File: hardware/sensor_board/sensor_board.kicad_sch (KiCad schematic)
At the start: 8 parts

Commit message: all bricked...
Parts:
- removed C? (x3): C, symbol Device:C
- removed R?: R, symbol Device:R
- removed U?: PESD2CAN, symbol ownLib:PESD2CAN
- added C1, C8: 10u / 10V, symbol Device:C
- added C2, C3, C7: 100n / 10V, symbol Device:C
- added C4, C5: 18p, symbol Device:C
- added C6: 1u / 10V, symbol Device:C
- added D1: RCLAMP0502BA, Package_TO_SOT_SMD:SOT-416, symbol Power_Protection:RCLAMP0502BA
- added J1: CORTEX-SWD-6, footprints:TC2030-IDC-NL, symbol ownLib:CORTEX-SWD-6
- added Q1, Q2: Q_NMOS_DGS, symbol Device:Q_PMOS_GSD
- added R1: 2k2, symbol Device:R
- added R2, R3, R4, R5: R, symbol Device:R
- added U1: ATSAMC21E17A, Package_DFN_QFN:QFN-32-1EP_5x5mm_P0.5mm_EP3.6x3.6mm, symbol ownLib:ATSAMC21E17A
- added Y1: Crystal, symbol Device:Crystal
- R6: renamed from R?; value R -> 120R
- gave numbers to parts that had none: 2
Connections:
- net CAN+: now also R6.2, U2.7 (CANH), D1.1 (K1)
- net CAN-: now also D1.2 (K2)
- net CAN_{RX}: now also U1.23 (PA24)
- net CAN_{TX}: now also U1.22 (PA23)
- net GND: now also C1.2, C2.2, C3.2, C4.1, C5.1, C6.2, C7.2, C8.2, D1.3 (A), J1.5 (GND), U1.10 (GND), U1.28 (GND)
- net VDD: now also C1.1, C2.1, C3.1, C8.1, J1.1 (VCC), Q2.2 (S), R1.1, R5.2, U1.30 (VDDIN), U1.9 (VDDANA)
- new net: Q2.1 (G), R3.2, R5.1
- new net: Q1.1 (G), R2.2, R4.1
- new net: C6.1, C7.1, U1.29 (VDDCORE)
- new net +5V: Q1.2 (S), R4.2
- new net 5VSW: Q1.3 (D)
- new net 5VSW_SIG: R2.1, U1.4 (PA03)
- new net CO2CAL: U1.6 (PA05)
- new net I2C.SCL: U1.12 (PA09)
- new net I2C.SDA: U1.11 (PA08)
- new net SWCLK: J1.4 (SWCLK), U1.31 (PA30)
- new net SWDIO: J1.2 (SWDIO), U1.32 (PA31)
- new net UART.RX: U1.2 (PA01)
- new net UART.TX: U1.1 (PA00)
- new net VDDSW: Q2.3 (D)
- new net VDDSW_SIG: R3.1, U1.5 (PA04)
- new net X_{IN}: C4.2, U1.15 (PA14), Y1.2
- new net X_{OUT}: C5.2, U1.16 (PA15), Y1.1
- new net ~{RESET}: J1.3 (nRESET), R1.2, U1.26 (~{RESET})
- no-connect marks 0 -> 14
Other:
- sheet Power ports: added none; removed SWD{SWO SWCLK SWDIO}
- moved on the sheet: J2, R6, U2

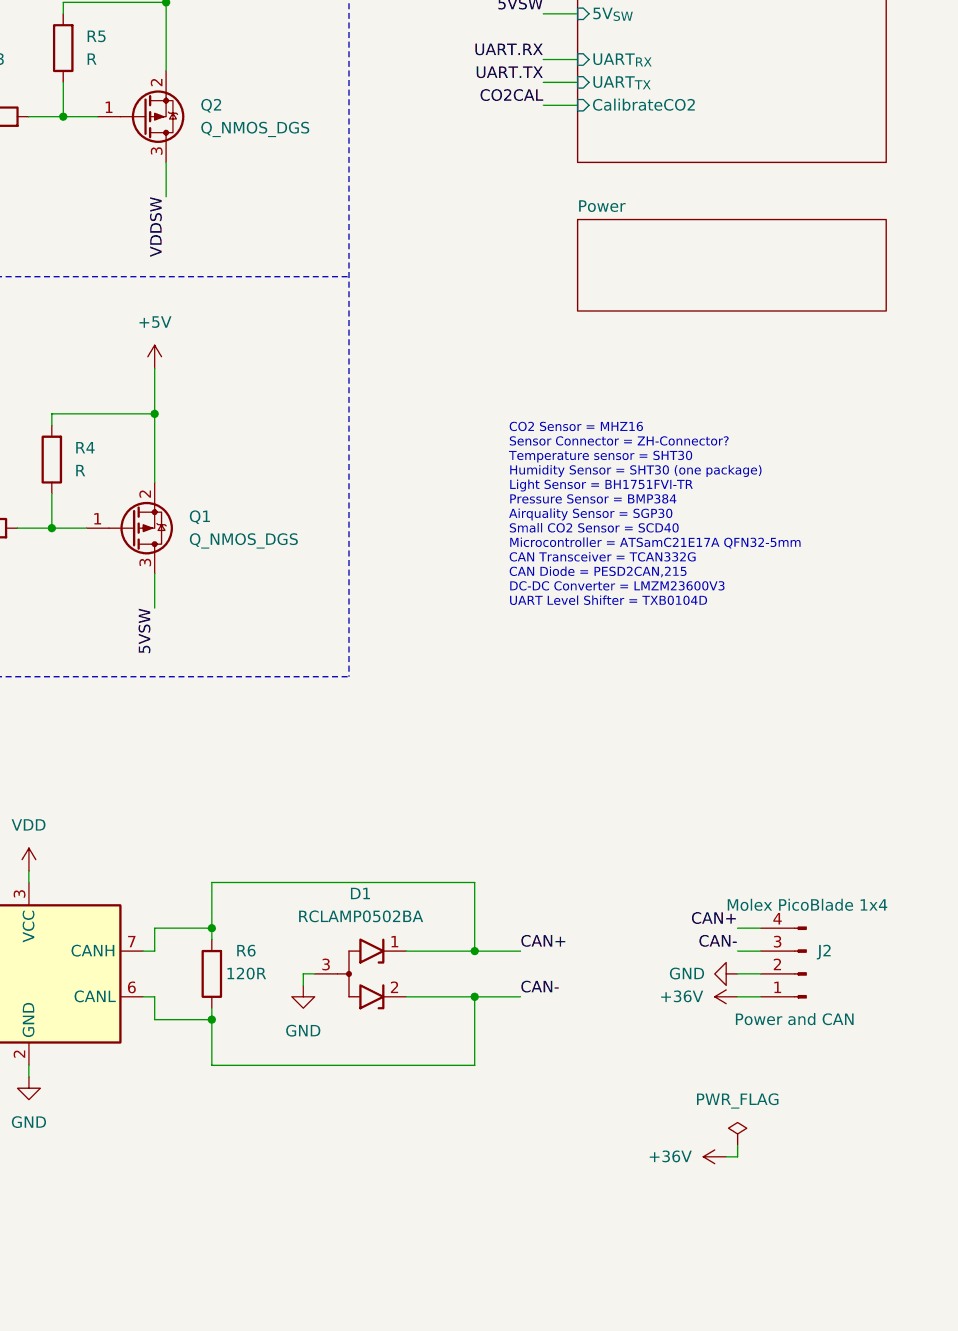
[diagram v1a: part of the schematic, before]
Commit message: solved issues with ERC
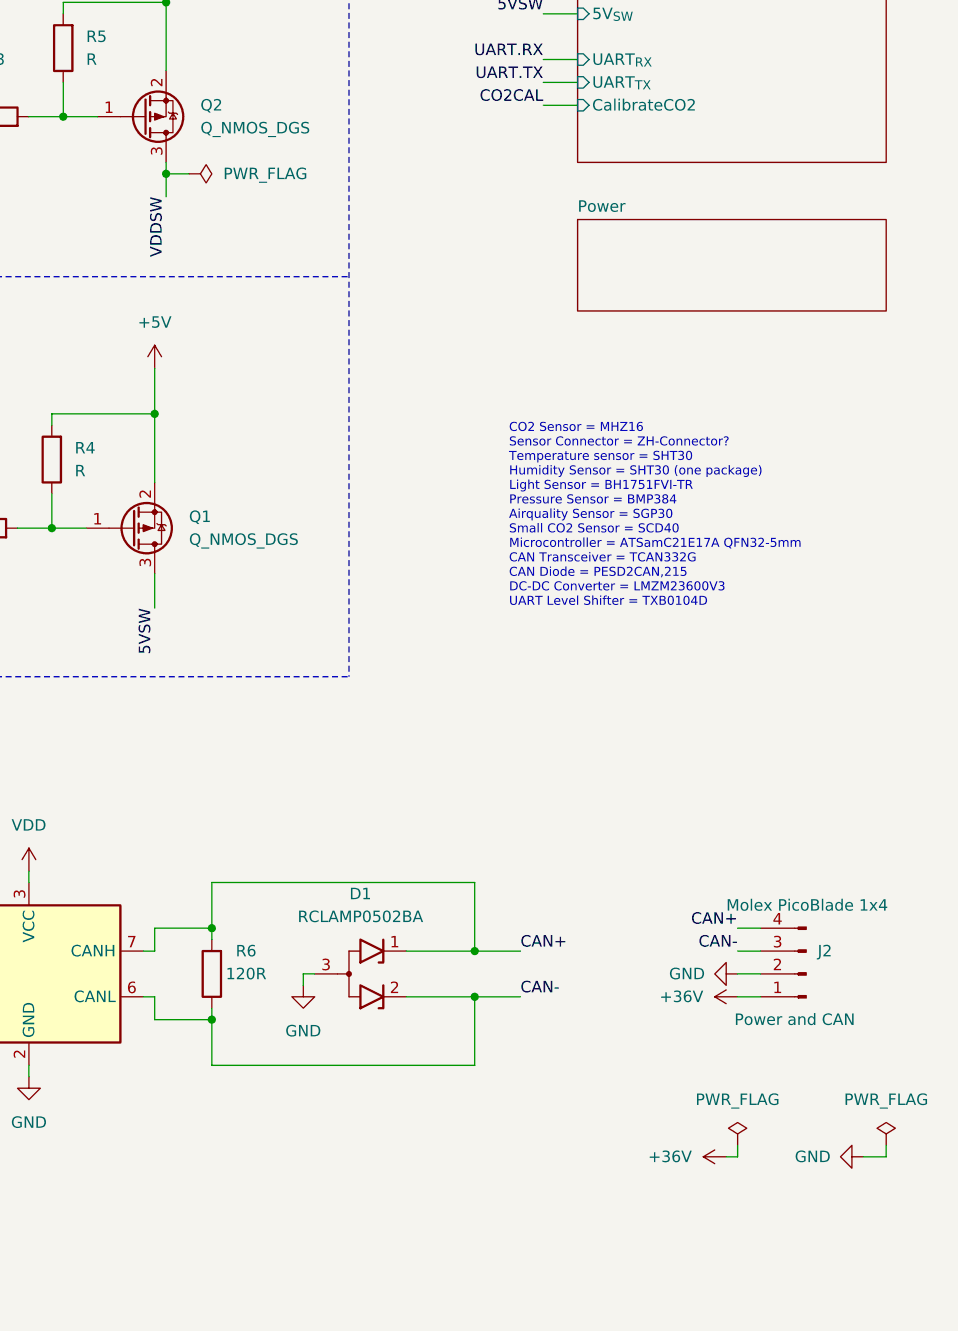
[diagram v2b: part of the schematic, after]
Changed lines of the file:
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@@
   (junction (at 193.04 80.01) (diameter 0) (color 0 0 0 0))
   (junction (at 194.31 34.29) (diameter 0) (color 0 0 0 0))
+  (junction (at 194.31 53.34) (diameter 0) (color 0 0 0 0))
   (junction (at 199.39 137.16) (diameter 0) (color 0 0 0 0))
   (junction (at 199.39 147.32) (diameter 0) (color 0 0 0 0))
@@
     (stroke (width 0) (type solid) (color 0 0 0 0))
   )
-  (wire (pts (xy 194.31 52.07) (xy 194.31 55.88))
+  (wire (pts (xy 194.31 52.07) (xy 194.31 53.34))
+    (stroke (width 0) (type solid) (color 0 0 0 0))
+  )
+  (wire (pts (xy 194.31 53.34) (xy 194.31 55.88))
+    (stroke (width 0) (type solid) (color 0 0 0 0))
+  )
+  (wire (pts (xy 194.31 53.34) (xy 196.85 53.34))
     (stroke (width 0) (type solid) (color 0 0 0 0))
   )
@@
   )
   (wire (pts (xy 257.81 162.56) (xy 257.81 161.29))
+    (stroke (width 0) (type solid) (color 0 0 0 0))
+  )
+  (wire (pts (xy 271.78 162.56) (xy 274.32 162.56))
+    (stroke (width 0) (type solid) (color 0 0 0 0))
+  )
+  (wire (pts (xy 274.32 162.56) (xy 274.32 161.29))
     (stroke (width 0) (type solid) (color 0 0 0 0))
   )
@@
     (pin "1")
   )
+  (symbol (lib_id "power:PWR_FLAG") (at 196.85 53.34 270) (unit 1)
+    (in_bom yes) (on_board yes) (fields_autoplaced)
+    (property "Reference" "#FLG01" (id 0) (at 198.755 53.34 0)
+      (effects (font (size 1.27 1.27)) hide)
+    )
+    (property "Value" "PWR_FLAG" (id 1) (at 200.66 53.3399 90)
+      (effects (font (size 1.27 1.27)) (justify left))
+    )
+    (property "Footprint" "" (id 2) (at 196.85 53.34 0)
+      (effects (font (size 1.27 1.27)) hide)
+    )
+    (property "Datasheet" "~" (id 3) (at 196.85 53.34 0)
+      (effects (font (size 1.27 1.27)) hide)
+    )
+    (pin "1")
+  )
   (symbol (lib_id "power:PWR_FLAG") (at 257.81 161.29 0) (unit 1)
     (in_bom yes) (on_board yes) (fields_autoplaced)
@@
     )
     (property "Datasheet" "~" (id 3) (at 257.81 161.29 0)
+      (effects (font (size 1.27 1.27)) hide)
+    )
+    (pin "1")
+  )
+  (symbol (lib_id "power:PWR_FLAG") (at 274.32 161.29 0) (unit 1)
+    (in_bom yes) (on_board yes) (fields_autoplaced)
+    (property "Reference" "#FLG0102" (id 0) (at 274.32 159.385 0)
+      (effects (font (size 1.27 1.27)) hide)
+    )
+    (property "Value" "PWR_FLAG" (id 1) (at 274.32 156.21 0))
+    (property "Footprint" "" (id 2) (at 274.32 161.29 0)
+      (effects (font (size 1.27 1.27)) hide)
+    )
+    (property "Datasheet" "~" (id 3) (at 274.32 161.29 0)
       (effects (font (size 1.27 1.27)) hide)
     )
@@
     )
     (property "Datasheet" "" (id 3) (at 257.81 142.24 0)
+      (effects (font (size 1.27 1.27)) hide)
+    )
+    (pin "1")
+  )
+  (symbol (lib_id "power:GND") (at 271.78 162.56 270) (unit 1)
+    (in_bom yes) (on_board yes)
+    (property "Reference" "#PWR0102" (id 0) (at 265.43 162.56 0)
+      (effects (font (size 1.27 1.27)) hide)
+    )
+    (property "Value" "GND" (id 1) (at 264.16 162.5599 90)
+      (effects (font (size 1.27 1.27)) (justify left))
+    )
+    (property "Footprint" "" (id 2) (at 271.78 162.56 0)
+      (effects (font (size 1.27 1.27)) hide)
+    )
+    (property "Datasheet" "" (id 3) (at 271.78 162.56 0)
       (effects (font (size 1.27 1.27)) hide)
     )
@@
   )
   (symbol_instances
+    (path "/3e86196d-7be5-4f72-a075-4619159f1c7f"
+      (reference "#FLG01") (unit 1) (value "PWR_FLAG") (footprint "")
+    )
     (path "/1d3ecf29-19a5-423b-9e86-10e11573b1b7"
       (reference "#FLG0101") (unit 1) (value "PWR_FLAG") (footprint "")
     )
+    (path "/74761b04-2e0e-48bc-8cd2-df69861a8420"
+      (reference "#FLG0102") (unit 1) (value "PWR_FLAG") (footprint "")
+    )
     (path "/8306a43a-0f6c-479d-b1d9-b6e95367aa2c"
       (reference "#PWR01") (unit 1) (value "VDD") (footprint "")
@@
       (reference "#PWR024") (unit 1) (value "GND") (footprint "")
     )
-    (path "/c4dbf479-cf2f-484d-ade6-def83986d8b6/b34e0c88-73d0-4fb3-a9d7-701d175303e9"
-      (reference "#PWR025") (unit 1) (value "VDD") (footprint "")
-    )
     (path "/c4dbf479-cf2f-484d-ade6-def83986d8b6/e44e48f3-3b0a-4d06-ba81-f082667f0867"
       (reference "#PWR026") (unit 1) (value "GND") (footprint "")
@@
       (reference "#PWR027") (unit 1) (value "GND") (footprint "")
     )
-    (path "/c4dbf479-cf2f-484d-ade6-def83986d8b6/c01d8e07-19b0-49c3-91c0-1c6475a0896f"
-      (reference "#PWR028") (unit 1) (value "VDD") (footprint "")
-    )
-    (path "/c4dbf479-cf2f-484d-ade6-def83986d8b6/fb54e666-356e-4647-8a05-d0c8bf4234d4"
-      (reference "#PWR029") (unit 1) (value "VDD") (footprint "")
-    )
     (path "/c4dbf479-cf2f-484d-ade6-def83986d8b6/811bdb1d-8b3c-44ab-924c-e552095907d7"
       (reference "#PWR030") (unit 1) (value "GND") (footprint "")
@@
       (reference "#PWR038") (unit 1) (value "GND") (footprint "")
     )
-    (path "/5266303c-cc26-4361-a3c7-41c3c779268d/5ea51cc6-628a-4b08-881b-78cf8dbcec67"
-      (reference "#PWR039") (unit 1) (value "VDD") (footprint "")
-    )
     (path "/adfd184c-f938-41aa-8cc3-19d2e60b847d"
       (reference "#PWR0101") (unit 1) (value "+36V") (footprint "")
     )
+    (path "/111fc8cc-7747-4f2e-9fcd-4c063190a483"
+      (reference "#PWR0102") (unit 1) (value "GND") (footprint "")
+    )
+    (path "/5266303c-cc26-4361-a3c7-41c3c779268d/4c9a339a-72e6-4346-b113-de4a084399ac"
+      (reference "#PWR0103") (unit 1) (value "+5V") (footprint "")
+    )
     (path "/cea51140-d1a5-4498-ac28-6d3c6af90a7f"
       (reference "C1") (unit 1) (value "10u / 10V") (footprint "")
@@
       (reference "U4") (unit 1) (value "SHT30-DIS") (footprint "Sensor_Humidity:Sensirion_DFN-8-1EP_2.5x2.5mm_P0.5mm_EP1.1x1.7mm")
     )
-    (path "/c4dbf479-cf2f-484d-ade6-def83986d8b6/2713ac11-4919-4bfe-87f5-9e015b3083d0"
-      (reference "U5") (unit 1) (value "BMP384") (footprint "")
-    )
-    (path "/c4dbf479-cf2f-484d-ade6-def83986d8b6/72869bcb-c605-4b0f-9b78-a3c7d0346b20"
-      (reference "U6") (unit 1) (value "SCD40") (footprint "")
-    )
-    (path "/c4dbf479-cf2f-484d-ade6-def83986d8b6/bcd0e211-90eb-41d5-bf7f-31ace572862e"
+    (path "/c4dbf479-cf2f-484d-ade6-def83986d8b6/f453ff1f-a773-45fc-ae5c-94711b2be9d1"
+      (reference "U5") (unit 1) (value "BMP384") (footprint "dp:BMP384")
+    )
+    (path "/c4dbf479-cf2f-484d-ade6-def83986d8b6/0afe84fd-9a71-4e85-ba4a-ded33ce31373"
+      (reference "U6") (unit 1) (value "SCD4x") (footprint "dp:SCD4x")
+    )
+    (path "/c4dbf479-cf2f-484d-ade6-def83986d8b6/0544bcc2-7380-4571-bf84-ab641f79cefc"
       (reference "U7") (unit 1) (value "SGP30") (footprint "")
     )

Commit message: did some stuff
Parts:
- C1, C2, C3, C4, C5, C6, C7, C8: footprint (none) -> Capacitor_SMD:C_0603_1608Metric
- J2: footprint (none) -> Connector_Molex:Molex_PicoBlade_53261-0471_1x04-1MP_P1.25mm_Horizontal
- Q1, Q2: value Q_NMOS_DGS -> SI2337DS-T1-BE3; footprint (none) -> Package_TO_SOT_SMD:SOT-23
- R1: footprint (none) -> Resistor_SMD:R_0603_1608Metric
- R2, R3: value R -> 100R; footprint (none) -> Resistor_SMD:R_0603_1608Metric
- R4, R5: value R -> 10k; footprint (none) -> Resistor_SMD:R_0603_1608Metric
- R6: footprint (none) -> Resistor_SMD:R_1206_3216Metric
- U2: footprint (none) -> Package_SO:SOIC-8_3.9x4.9mm_P1.27mm
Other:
- moved on the sheet: Q1, Q2, R2, R3, R4, R5

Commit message: finished schematic and added board
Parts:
- added H1, H2, H3, H4: MountingHole, MountingHole:MountingHole_3.2mm_M3, symbol Mechanical:MountingHole
- J1: footprint footprints:TC2030-IDC-NL -> Connector_Hirose:Hirose_DF11-6DP-2DSA_2x03_P2.00mm_Vertical
- Y1: footprint (none) -> ownLib:Abracon_ABC2
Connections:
- net CAN+: now also J2.3 (Pin_3); no longer J2.4 (Pin_4)
- net CAN-: now also J2.4 (Pin_4); no longer J2.3 (Pin_3)
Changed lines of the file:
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@@
     (effects (font (size 1.27 1.27)) (justify right bottom))
   )
-  (label "CAN+" (at 257.81 137.16 180)
+  (label "CAN-" (at 257.81 137.16 180)
     (effects (font (size 1.27 1.27)) (justify right bottom))
   )
-  (label "CAN-" (at 257.81 139.7 180)
+  (label "CAN+" (at 257.81 139.7 180)
     (effects (font (size 1.27 1.27)) (justify right bottom))
   )
@@
     (pin "1")
   )
+  (symbol (lib_id "Mechanical:MountingHole") (at 158.75 177.8 0) (unit 1)
+    (in_bom yes) (on_board yes) (fields_autoplaced)
+    (property "Reference" "H1" (id 0) (at 161.29 176.5299 0)
+      (effects (font (size 1.27 1.27)) (justify left))
+    )
+    (property "Value" "MountingHole" (id 1) (at 161.29 179.0699 0)
+      (effects (font (size 1.27 1.27)) (justify left))
+    )
+    (property "Footprint" "MountingHole:MountingHole_3.2mm_M3" (id 2) (at 158.75 177.8 0)
+      (effects (font (size 1.27 1.27)) hide)
+    )
+    (property "Datasheet" "~" (id 3) (at 158.75 177.8 0)
+      (effects (font (size 1.27 1.27)) hide)
+    )
+  )
+  (symbol (lib_id "Mechanical:MountingHole") (at 158.75 182.88 0) (unit 1)
+    (in_bom yes) (on_board yes) (fields_autoplaced)
+    (property "Reference" "H2" (id 0) (at 161.29 181.6099 0)
+      (effects (font (size 1.27 1.27)) (justify left))
+    )
+    (property "Value" "MountingHole" (id 1) (at 161.29 184.1499 0)
+      (effects (font (size 1.27 1.27)) (justify left))
+    )
+    (property "Footprint" "MountingHole:MountingHole_3.2mm_M3" (id 2) (at 158.75 182.88 0)
+      (effects (font (size 1.27 1.27)) hide)
+    )
+    (property "Datasheet" "~" (id 3) (at 158.75 182.88 0)
+      (effects (font (size 1.27 1.27)) hide)
+    )
+  )
+  (symbol (lib_id "Mechanical:MountingHole") (at 158.75 187.96 0) (unit 1)
+    (in_bom yes) (on_board yes) (fields_autoplaced)
+    (property "Reference" "H3" (id 0) (at 161.29 186.6899 0)
+      (effects (font (size 1.27 1.27)) (justify left))
+    )
+    (property "Value" "MountingHole" (id 1) (at 161.29 189.2299 0)
+      (effects (font (size 1.27 1.27)) (justify left))
+    )
+    (property "Footprint" "MountingHole:MountingHole_3.2mm_M3" (id 2) (at 158.75 187.96 0)
+      (effects (font (size 1.27 1.27)) hide)
+    )
+    (property "Datasheet" "~" (id 3) (at 158.75 187.96 0)
+      (effects (font (size 1.27 1.27)) hide)
+    )
+  )
+  (symbol (lib_id "Mechanical:MountingHole") (at 158.75 193.04 0) (unit 1)
+    (in_bom yes) (on_board yes) (fields_autoplaced)
+    (property "Reference" "H4" (id 0) (at 161.29 191.7699 0)
+      (effects (font (size 1.27 1.27)) (justify left))
+    )
+    (property "Value" "MountingHole" (id 1) (at 161.29 194.3099 0)
+      (effects (font (size 1.27 1.27)) (justify left))
+    )
+    (property "Footprint" "MountingHole:MountingHole_3.2mm_M3" (id 2) (at 158.75 193.04 0)
+      (effects (font (size 1.27 1.27)) hide)
+    )
+    (property "Datasheet" "~" (id 3) (at 158.75 193.04 0)
+      (effects (font (size 1.27 1.27)) hide)
+    )
+  )
   (symbol (lib_id "Device:R") (at 40.64 160.02 0) (unit 1)
     (in_bom yes) (on_board yes) (fields_autoplaced)
@@
       (effects (font (size 1.27 1.27)) (justify right))
     )
-    (property "Footprint" "" (id 2) (at 109.22 166.37 0)
+    (property "Footprint" "ownLib:Abracon_ABC2" (id 2) (at 109.22 166.37 0)
       (effects (font (size 1.27 1.27)) hide)
     )
@@
     (property "Reference" "J1" (id 0) (at 57.15 181.61 0))
     (property "Value" "CORTEX-SWD-6" (id 1) (at 57.15 179.07 0))
-    (property "Footprint" "footprints:TC2030-IDC-NL" (id 2) (at 53.34 168.91 0)
+    (property "Footprint" "Connector_Hirose:Hirose_DF11-6DP-2DSA_2x03_P2.00mm_Vertical" (id 2) (at 53.34 168.91 0)
       (effects (font (size 1.27 1.27)) hide)
     )
@@
       (reference "#PWR021") (unit 1) (value "GND") (footprint "")
     )
-    (path "/c4dbf479-cf2f-484d-ade6-def83986d8b6/f67a32d3-7511-4d61-99b5-d4663f0b0e44"
-      (reference "#PWR022") (unit 1) (value "VDD") (footprint "")
-    )
     (path "/c4dbf479-cf2f-484d-ade6-def83986d8b6/3e6e17d9-50a2-42ca-8d07-88996d701999"
       (reference "#PWR023") (unit 1) (value "GND") (footprint "")
@@
       (reference "D1") (unit 1) (value "RCLAMP0502BA") (footprint "Package_TO_SOT_SMD:SOT-416")
     )
+    (path "/371c1c85-29c4-4430-a166-296c236cc67f"
+      (reference "H1") (unit 1) (value "MountingHole") (footprint "MountingHole:MountingHole_3.2mm_M3")
+    )
+    (path "/4d860418-d4f7-4302-a4cf-daec800bb6e8"
+      (reference "H2") (unit 1) (value "MountingHole") (footprint "MountingHole:MountingHole_3.2mm_M3")
+    )
+    (path "/648b5ea9-7fe1-4e55-b698-997506f54bc4"
+      (reference "H3") (unit 1) (value "MountingHole") (footprint "MountingHole:MountingHole_3.2mm_M3")
+    )
+    (path "/70c8d3a6-3703-44a2-bf2b-3ec103e9d4e7"
+      (reference "H4") (unit 1) (value "MountingHole") (footprint "MountingHole:MountingHole_3.2mm_M3")
+    )
     (path "/b6cc8769-7f16-4930-8036-bf1adcf0d5e5"
-      (reference "J1") (unit 1) (value "CORTEX-SWD-6") (footprint "footprints:TC2030-IDC-NL")
+      (reference "J1") (unit 1) (value "CORTEX-SWD-6") (footprint "Connector_Hirose:Hirose_DF11-6DP-2DSA_2x03_P2.00mm_Vertical")
     )
     (path "/7e8eaa66-5102-45f3-bcc4-3b227ec0eb1c"
@@
     )
     (path "/c4dbf479-cf2f-484d-ade6-def83986d8b6/921066e0-977a-4ced-abaa-e12813cdb4e7"
-      (reference "U8") (unit 1) (value "BH1751FVI") (footprint "")
+      (reference "U8") (unit 1) (value "BH1751FVI") (footprint "ownLib:WSOF6")
     )
     (path "/5266303c-cc26-4361-a3c7-41c3c779268d/6cf22af1-c336-4ca9-a76a-49f84b20a29e"
@@
     )
     (path "/3dffc84b-d31c-4efc-9582-d54f9860c01b"
-      (reference "Y1") (unit 1) (value "Crystal") (footprint "")
-    )
-  )
+      (reference "Y1") (unit 1) (value "Crystal") (footprint "ownLib:Abracon_ABC2")
+    )
+  )

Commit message: review
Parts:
- removed H1, H2, H3, H4: MountingHole, MountingHole:MountingHole_3.2mm_M3, symbol Mechanical:MountingHole
- added C?: 10nF / 6.3V, Capacitor_SMD:C_0603_1608Metric, symbol Device:C
- added R?: 10k, Resistor_SMD:R_0603_1608Metric, symbol Device:R
- added R?: 100k, Resistor_SMD:R_0603_1608Metric, symbol Device:R
- C1, C8: value 10u / 10V -> 10u / 6.3V
- C2, C3, C7: value 100n / 10V -> 100n / 50V
- C6: value 1u / 10V -> 1u / 6.3V
- R1: value 2k2 -> 10k
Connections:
- net +36V: now also J2.2 (Pin_2); no longer J2.1 (Pin_1)
- net GND: now also J2.1 (Pin_1), C?.1; no longer J2.2 (Pin_2)
- net SWCLK: now also R?.2
- net SWDIO: now also R?.2
- net VDD: now also R?.1, R?.1
- net ~{RESET}: now also C?.2
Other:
- note added: "CAP 10uf 100nf"
- note added: "Calculate Cs correctly! Parasitic: Xin 5.9 pF Xout 3.1 pF"
- note added: "Pins wrong! Right pins: 1 SWO 2 GND 3 SWCLK 5 SWDIO 4 ~{RESET} 6 3.3V"
- moved on the sheet: C4, C5, C6, C7, Y1
